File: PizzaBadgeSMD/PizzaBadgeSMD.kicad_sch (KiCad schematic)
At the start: 168 parts, among them J1 BAT -, J2 BAT +, Q1 NPN, Q2 NPN, Q3 NPN, Q4 NPN, Q5 NPN, Q6 NPN, Q7 NPN, Q8 NPN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

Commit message: update SMD version
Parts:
- added R82, R83: 10K, Resistor_SMD:R_0805_2012Metric, symbol Device:R
- Q1, Q2, Q3, Q4, Q5, Q6, Q7, Q8: symbol Device:Q_NPN_EBC -> Device:Q_NPN_BEC
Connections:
- net 3.3V: now also R82.1
- net GND: now also R83.2
- net SLICE_8: now also R83.1
- net at R61.2, R62.2, R63.2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: now also Q7.2 (E); no longer Q7.1 (E)
- net at R71.2, R72.2, R73.2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: now also Q8.2 (E); no longer Q8.1 (E)
- net at R80.1: now also Q8.1 (B); no longer Q8.2 (B)
- net at R30.1: now also Q3.1 (B); no longer Q3.2 (B)
- net at R39.1: now also Q4.1 (B); no longer Q4.2 (B)
- net at R41.2, R42.2, R43.2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: now also Q5.2 (E); no longer Q5.1 (E)
- net at R21.2, R22.2, R23.2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: now also Q3.2 (E); no longer Q3.1 (E)
- net at R51.2, R52.2, R53.2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: now also Q6.2 (E); no longer Q6.1 (E)
- net at R11.2, R12.2, R13.2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: now also Q2.2 (E); no longer Q2.1 (E)
- net at R20.1: now also Q2.1 (B); no longer Q2.2 (B)
- net at R31.2, R32.2, R33.2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: now also Q4.2 (E); no longer Q4.1 (E)
- net at R50.1: now also Q5.1 (B); no longer Q5.2 (B)
- net at R1.2, R2.2, R3.2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: now also Q1.2 (E); no longer Q1.1 (E)
- net at R60.1: now also Q6.1 (B); no longer Q6.2 (B)
- net at R10.1: now also Q1.1 (B); no longer Q1.2 (B)
- net at R70.1: now also Q7.1 (B); no longer Q7.2 (B)
- net at U1.3 (EN): now also R82.2
- no-connect marks 11 -> 10
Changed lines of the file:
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@@
   (junction (at 143.51 176.53) (diameter 0) (color 0 0 0 0)
   )
+  (junction (at 269.24 146.05) (diameter 0) (color 0 0 0 0)
+  )
   (junction (at 161.29 120.65) (diameter 0) (color 0 0 0 0)
   )
@@
   (no_connect (at 234.95 146.05))
   (no_connect (at 234.95 138.43))
-  (no_connect (at 234.95 128.27))
   (no_connect (at 265.43 130.81))
   (wire (pts (xy 227.33 54.61) (xy 227.33 62.23))
@@
     (stroke (width 0) (type default) (color 0 0 0 0))
   )
+  (wire (pts (xy 269.24 146.05) (xy 269.24 152.4))
+    (stroke (width 0) (type default) (color 0 0 0 0))
+  )
   (wire (pts (xy 21.59 29.21) (xy 21.59 36.83))
     (stroke (width 0) (type default) (color 0 0 0 0))
@@
     (stroke (width 0) (type default) (color 0 0 0 0))
   )
+  (wire (pts (xy 279.4 152.4) (xy 276.86 152.4))
+    (stroke (width 0) (type default) (color 0 0 0 0))
+  )
   (wire (pts (xy 123.19 29.21) (xy 121.92 29.21))
     (stroke (width 0) (type default) (color 0 0 0 0))
@@
     (stroke (width 0) (type default) (color 0 0 0 0))
   )
+  (wire (pts (xy 269.24 146.05) (xy 265.43 146.05))
+    (stroke (width 0) (type default) (color 0 0 0 0))
+  )
   (wire (pts (xy 71.12 85.09) (xy 69.85 85.09))
     (stroke (width 0) (type default) (color 0 0 0 0))
@@
     (stroke (width 0) (type default) (color 0 0 0 0))
   )
+  (wire (pts (xy 271.78 146.05) (xy 269.24 146.05))
+    (stroke (width 0) (type default) (color 0 0 0 0))
+  )
   (wire (pts (xy 92.71 134.62) (xy 93.98 134.62))
     (stroke (width 0) (type default) (color 0 0 0 0))
@@
     (stroke (width 0) (type default) (color 0 0 0 0))
   )
+  (global_label "3.3V" (shape input) (at 227.33 128.27 180) (fields_autoplaced)
+    (effects (font (size 1.27 1.27)) (justify right))
+    (property "Intersheet References" "${INTERSHEET_REFS}" (id 0) (at 220.8045 128.3494 0)
+      (effects (font (size 1.27 1.27)) (justify right) hide)
+    )
+  )
   (global_label "GND" (shape input) (at 69.85 90.17 180) (fields_autoplaced)
     (effects (font (size 1.27 1.27)) (justify right))
@@
     )
   )
+  (global_label "GND" (shape input) (at 279.4 152.4 270) (fields_autoplaced)
+    (effects (font (size 1.27 1.27)) (justify right))
+    (property "Intersheet References" "${INTERSHEET_REFS}" (id 0) (at 279.3206 158.6836 90)
+      (effects (font (size 1.27 1.27)) (justify right) hide)
+    )
+  )
   (global_label "SLICE_3" (shape input) (at 265.43 123.19 0) (fields_autoplaced)
     (effects (font (size 1.27 1.27)) (justify left))
@@
     )
   )
-  (global_label "SLICE_8" (shape input) (at 265.43 146.05 0) (fields_autoplaced)
+  (global_label "SLICE_8" (shape input) (at 271.78 146.05 0) (fields_autoplaced)
     (effects (font (size 1.27 1.27)) (justify left))
-    (property "Intersheet References" "${INTERSHEET_REFS}" (id 0) (at 275.2817 145.9706 0)
+    (property "Intersheet References" "${INTERSHEET_REFS}" (id 0) (at 281.6317 145.9706 0)
       (effects (font (size 1.27 1.27)) (justify left) hide)
     )
@@
     (pin "2")
   )
-  (symbol (lib_id "Device:Q_NPN_EBC") (at 167.64 140.97 270) (unit 1)
+  (symbol (lib_id "Device:Q_NPN_BEC") (at 167.64 140.97 270) (unit 1)
     (in_bom yes) (on_board yes) (fields_autoplaced)
     (property "Reference" "Q8" (id 0) (at 167.64 147.32 90))
@@
     (pin "2")
   )
-  (symbol (lib_id "Device:Q_NPN_EBC") (at 96.52 49.53 270) (unit 1)
+  (symbol (lib_id "Device:Q_NPN_BEC") (at 96.52 49.53 270) (unit 1)
     (in_bom yes) (on_board yes) (fields_autoplaced)
     (property "Reference" "Q2" (id 0) (at 96.52 55.88 90))
@@
     (pin "2")
   )
-  (symbol (lib_id "Device:Q_NPN_EBC") (at 194.31 49.53 270) (unit 1)
+  (symbol (lib_id "Device:Q_NPN_BEC") (at 194.31 49.53 270) (unit 1)
     (in_bom yes) (on_board yes) (fields_autoplaced)
     (property "Reference" "Q4" (id 0) (at 194.31 55.88 90))
@@
     (pin "1")
   )
-  (symbol (lib_id "Device:Q_NPN_EBC") (at 146.05 49.53 270) (unit 1)
+  (symbol (lib_id "Device:Q_NPN_BEC") (at 146.05 49.53 270) (unit 1)
     (in_bom yes) (on_board yes) (fields_autoplaced)
     (property "Reference" "Q3" (id 0) (at 146.05 55.88 90))
@@
     (pin "2")
   )
-  (symbol (lib_id "Device:Q_NPN_EBC") (at 251.46 52.07 270) (unit 1)
+  (symbol (lib_id "Device:Q_NPN_BEC") (at 251.46 52.07 270) (unit 1)
     (in_bom yes) (on_board yes) (fields_autoplaced)
     (property "Reference" "Q5" (id 0) (at 251.46 58.42 90))
@@
     (pin "2")
   )
-  (symbol (lib_id "Device:Q_NPN_EBC") (at 54.61 139.7 270) (unit 1)
+  (symbol (lib_id "Device:Q_NPN_BEC") (at 54.61 139.7 270) (unit 1)
     (in_bom yes) (on_board yes) (fields_autoplaced)
     (property "Reference" "Q6" (id 0) (at 54.61 146.05 90))
@@
     (pin "2")
   )
-  (symbol (lib_id "Device:Q_NPN_EBC") (at 107.95 139.7 270) (unit 1)
+  (symbol (lib_id "Device:Q_NPN_BEC") (at 107.95 139.7 270) (unit 1)
     (in_bom yes) (on_board yes) (fields_autoplaced)
     (property "Reference" "Q7" (id 0) (at 107.95 146.05 90))
@@
     (pin "2")
   )
-  (symbol (lib_id "Device:Q_NPN_EBC") (at 46.99 49.53 270) (unit 1)
+  (symbol (lib_id "Device:Q_NPN_BEC") (at 46.99 49.53 270) (unit 1)
     (in_bom yes) (on_board yes) (fields_autoplaced)
     (property "Reference" "Q1" (id 0) (at 46.99 55.88 90))
@@
     (pin "2")
   )
+  (symbol (lib_id "Device:R") (at 231.14 128.27 90) (unit 1)
+    (in_bom yes) (on_board yes)
+    (property "Reference" "R82" (id 0) (at 231.14 125.73 90))
+    (property "Value" "10K" (id 1) (at 231.14 128.27 90))
+    (property "Footprint" "Resistor_SMD:R_0805_2012Metric" (id 2) (at 231.14 130.048 90)
+      (effects (font (size 1.27 1.27)) hide)
+    )
+    (property "Datasheet" "~" (id 3) (at 231.14 128.27 0)
+      (effects (font (size 1.27 1.27)) hide)
+    )
+    (pin "1")
+    (pin "2")
+  )
   (symbol (lib_id "Device:R") (at 44.45 149.86 90) (unit 1)
     (in_bom yes) (on_board yes)
@@
     (pin "2")
   )
+  (symbol (lib_id "Device:R") (at 273.05 152.4 90) (unit 1)
+    (in_bom yes) (on_board yes)
+    (property "Reference" "R83" (id 0) (at 273.05 149.86 90))
+    (property "Value" "10K" (id 1) (at 273.05 152.4 90))
+    (property "Footprint" "Resistor_SMD:R_0805_2012Metric" (id 2) (at 273.05 154.178 90)
+      (effects (font (size 1.27 1.27)) hide)
+    )
+    (property "Datasheet" "~" (id 3) (at 273.05 152.4 0)
+      (effects (font (size 1.27 1.27)) hide)
+    )
+    (pin "1")
+    (pin "2")
+  )
   (symbol (lib_id "Device:R") (at 157.48 167.64 90) (unit 1)
     (in_bom yes) (on_board yes)
@@
       (reference "R81") (unit 1) (value "10K") (footprint "Resistor_SMD:R_0805_2012Metric")
     )
+    (path "/f0d89eae-86d0-4eee-82c6-ad3daf7543e5"
+      (reference "R82") (unit 1) (value "10K") (footprint "Resistor_SMD:R_0805_2012Metric")
+    )
+    (path "/f377b136-56b5-4e23-8cd2-f732b5942e28"
+      (reference "R83") (unit 1) (value "10K") (footprint "Resistor_SMD:R_0805_2012Metric")
+    )
     (path "/ed6cd72f-4985-4265-a8c6-e1402f632187"

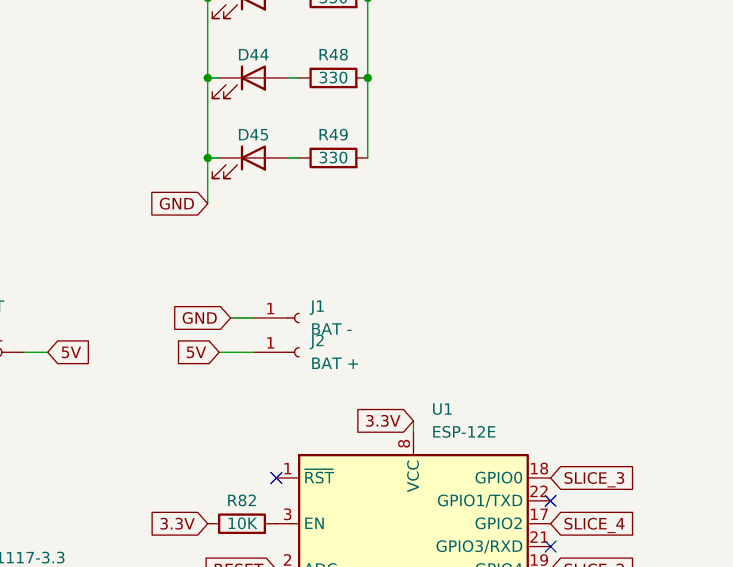
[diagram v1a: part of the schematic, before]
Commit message: add coin battery
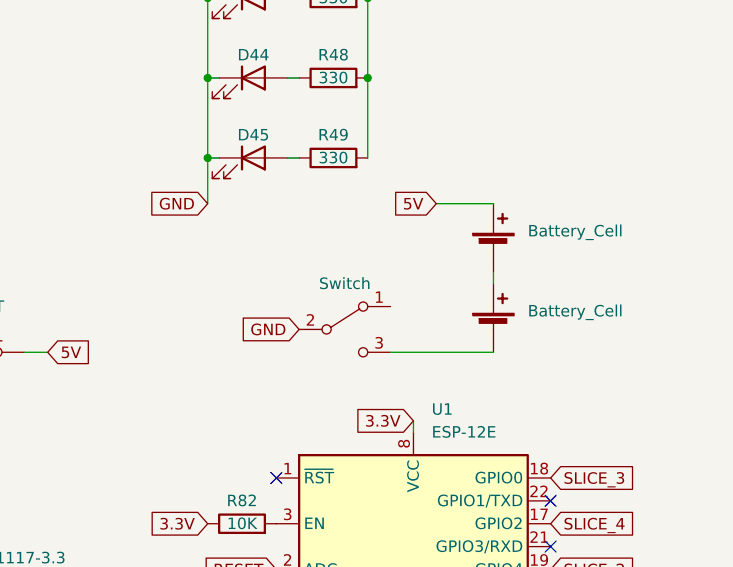
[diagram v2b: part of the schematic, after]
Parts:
- removed J1: BAT -, TestPoint:TestPoint_Pad_3.0x3.0mm, symbol Connector:Conn_01x01_Female
- removed J2: BAT +, TestPoint:TestPoint_Pad_3.0x3.0mm, symbol Connector:Conn_01x01_Female
- added BT1, BT2: Battery_Cell, Battery:BatteryHolder_Keystone_3000_1x12mm, symbol Device:Battery_Cell
- added SW2: Switch, Button_Switch_SMD:SW_SPDT_CK-JS102011SAQN, symbol Switch:SW_SPDT
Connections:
- net 5V: now also BT1.1 (+)
- net GND: now also SW2.2 (B)
- new net: BT1.2 (-), BT2.1 (+)
- new net: BT2.2 (-), SW2.3 (C)
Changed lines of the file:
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@@
     (stroke (width 0) (type default) (color 0 0 0 0))
   )
+  (wire (pts (xy 259.08 100.33) (xy 259.08 101.6))
+    (stroke (width 0) (type default) (color 0 0 0 0))
+  )
   (wire (pts (xy 78.74 67.31) (xy 80.01 67.31))
     (stroke (width 0) (type default) (color 0 0 0 0))
@@
     (stroke (width 0) (type default) (color 0 0 0 0))
   )
+  (wire (pts (xy 252.73 92.71) (xy 259.08 92.71))
+    (stroke (width 0) (type default) (color 0 0 0 0))
+  )
   (wire (pts (xy 170.18 44.45) (xy 170.18 52.07))
     (stroke (width 0) (type default) (color 0 0 0 0))
@@
     (stroke (width 0) (type default) (color 0 0 0 0))
   )
-  (wire (pts (xy 229.87 105.41) (xy 232.41 105.41))
-    (stroke (width 0) (type default) (color 0 0 0 0))
-  )
   (wire (pts (xy 205.74 143.51) (xy 205.74 146.05))
     (stroke (width 0) (type default) (color 0 0 0 0))
@@
     (stroke (width 0) (type default) (color 0 0 0 0))
   )
-  (wire (pts (xy 228.6 109.22) (xy 232.41 109.22))
-    (stroke (width 0) (type default) (color 0 0 0 0))
-  )
   (wire (pts (xy 101.6 166.37) (xy 101.6 175.26))
     (stroke (width 0) (type default) (color 0 0 0 0))
@@
     (stroke (width 0) (type default) (color 0 0 0 0))
   )
+  (wire (pts (xy 247.65 109.22) (xy 259.08 109.22))
+    (stroke (width 0) (type default) (color 0 0 0 0))
+  )
   (wire (pts (xy 78.74 29.21) (xy 80.01 29.21))
     (stroke (width 0) (type default) (color 0 0 0 0))
@@
     )
   )
-  (global_label "GND" (shape input) (at 229.87 105.41 180) (fields_autoplaced)
+  (global_label "GND" (shape input) (at 237.49 106.68 180) (fields_autoplaced)
     (effects (font (size 1.27 1.27)) (justify right))
-    (property "Intersheet References" "${INTERSHEET_REFS}" (id 0) (at 223.5864 105.3306 0)
+    (property "Intersheet References" "${INTERSHEET_REFS}" (id 0) (at 231.2064 106.6006 0)
       (effects (font (size 1.27 1.27)) (justify right) hide)
     )
@@
     )
   )
-  (global_label "5V" (shape input) (at 228.6 109.22 180) (fields_autoplaced)
+  (global_label "5V" (shape input) (at 252.73 92.71 180) (fields_autoplaced)
     (effects (font (size 1.27 1.27)) (justify right))
-    (property "Intersheet References" "${INTERSHEET_REFS}" (id 0) (at 223.8888 109.1406 0)
+    (property "Intersheet References" "${INTERSHEET_REFS}" (id 0) (at 248.0188 92.6306 0)
       (effects (font (size 1.27 1.27)) (justify right) hide)
     )
@@
     (pin "2")
   )
-  (symbol (lib_id "Connector:Conn_01x01_Female") (at 237.49 109.22 0) (unit 1)
-    (in_bom yes) (on_board yes) (fields_autoplaced)
-    (property "Reference" "J2" (id 0) (at 238.76 107.9499 0)
-      (effects (font (size 1.27 1.27)) (justify left))
-    )
-    (property "Value" "BAT +" (id 1) (at 238.76 110.4899 0)
-      (effects (font (size 1.27 1.27)) (justify left))
-    )
-    (property "Footprint" "TestPoint:TestPoint_Pad_3.0x3.0mm" (id 2) (at 237.49 109.22 0)
-      (effects (font (size 1.27 1.27)) hide)
-    )
-    (property "Datasheet" "~" (id 3) (at 237.49 109.22 0)
-      (effects (font (size 1.27 1.27)) hide)
-    )
-    (pin "1")
-  )
   (symbol (lib_id "Device:Q_NPN_BEC") (at 146.05 49.53 270) (unit 1)
     (in_bom yes) (on_board yes) (fields_autoplaced)
@@
     (pin "2")
   )
+  (symbol (lib_id "Device:Battery_Cell") (at 259.08 97.79 0) (unit 1)
+    (in_bom yes) (on_board yes) (fields_autoplaced)
+    (property "Reference" "BT1" (id 0) (at 262.89 94.4879 0)
+      (effects (font (size 1.27 1.27)) (justify left) hide)
+    )
+    (property "Value" "Battery_Cell" (id 1) (at 262.89 95.7579 0)
+      (effects (font (size 1.27 1.27)) (justify left))
+    )
+    (property "Footprint" "Battery:BatteryHolder_Keystone_3000_1x12mm" (id 2) (at 259.08 96.266 90)
+      (effects (font (size 1.27 1.27)) hide)
+    )
+    (property "Datasheet" "~" (id 3) (at 259.08 96.266 90)
+      (effects (font (size 1.27 1.27)) hide)
+    )
+    (pin "1")
+    (pin "2")
+  )
   (symbol (lib_id "Device:R") (at 58.42 132.08 90) (unit 1)
     (in_bom yes) (on_board yes)
@@
     (pin "2")
   )
-  (symbol (lib_id "Connector:Conn_01x01_Female") (at 237.49 105.41 0) (unit 1)
-    (in_bom yes) (on_board yes) (fields_autoplaced)
-    (property "Reference" "J1" (id 0) (at 238.76 104.1399 0)
-      (effects (font (size 1.27 1.27)) (justify left))
-    )
-    (property "Value" "BAT -" (id 1) (at 238.76 106.6799 0)
-      (effects (font (size 1.27 1.27)) (justify left))
-    )
-    (property "Footprint" "TestPoint:TestPoint_Pad_3.0x3.0mm" (id 2) (at 237.49 105.41 0)
-      (effects (font (size 1.27 1.27)) hide)
-    )
-    (property "Datasheet" "~" (id 3) (at 237.49 105.41 0)
-      (effects (font (size 1.27 1.27)) hide)
-    )
-    (pin "1")
-  )
   (symbol (lib_id "Device:LED") (at 175.26 44.45 0) (unit 1)
     (in_bom yes) (on_board yes)
@@
     (pin "2")
   )
+  (symbol (lib_id "Device:Battery_Cell") (at 259.08 106.68 0) (unit 1)
+    (in_bom yes) (on_board yes) (fields_autoplaced)
+    (property "Reference" "BT2" (id 0) (at 262.89 103.3779 0)
+      (effects (font (size 1.27 1.27)) (justify left) hide)
+    )
+    (property "Value" "Battery_Cell" (id 1) (at 262.89 104.6479 0)
+      (effects (font (size 1.27 1.27)) (justify left))
+    )
+    (property "Footprint" "Battery:BatteryHolder_Keystone_3000_1x12mm" (id 2) (at 259.08 105.156 90)
+      (effects (font (size 1.27 1.27)) hide)
+    )
+    (property "Datasheet" "~" (id 3) (at 259.08 105.156 90)
+      (effects (font (size 1.27 1.27)) hide)
+    )
+    (pin "1")
+    (pin "2")
+  )
   (symbol (lib_id "Device:LED") (at 35.56 119.38 0) (unit 1)
     (in_bom yes) (on_board yes)
@@
     (pin "2")
   )
+  (symbol (lib_id "Switch:SW_SPDT") (at 242.57 106.68 0) (unit 1)
+    (in_bom yes) (on_board yes) (fields_autoplaced)
+    (property "Reference" "SW2" (id 0) (at 242.57 101.6 0)
+      (effects (font (size 1.27 1.27)) hide)
+    )
+    (property "Value" "Switch" (id 1) (at 242.57 101.6 0))
+    (property "Footprint" "Button_Switch_SMD:SW_SPDT_CK-JS102011SAQN" (id 2) (at 242.57 106.68 0)
+      (effects (font (size 1.27 1.27)) hide)
+    )
+    (property "Datasheet" "~" (id 3) (at 242.57 106.68 0)
+      (effects (font (size 1.27 1.27)) hide)
+    )
+    (pin "1")
+    (pin "2")
+    (pin "3")
+  )
   (symbol (lib_id "Device:R") (at 157.48 167.64 90) (unit 1)
     (in_bom yes) (on_board yes)
@@
   )
   (symbol_instances
+    (path "/6c827c18-fa9e-48ed-ae59-de7f06672e71"
+      (reference "BT1") (unit 1) (value "Battery_Cell") (footprint "Battery:BatteryHolder_Keystone_3000_1x12mm")
+    )
+    (path "/d7672da8-9302-4479-abcf-93a65f594d80"
+      (reference "BT2") (unit 1) (value "Battery_Cell") (footprint "Battery:BatteryHolder_Keystone_3000_1x12mm")
+    )
     (path "/d4fba0db-5d79-4a75-b55a-6213bf0452ed"
       (reference "C1") (unit 1) (value "1uF") (footprint "Capacitor_SMD:C_0805_2012Metric")
@@
       (reference "D72") (unit 1) (value "LED") (footprint "LED_SMD:LED_0805_2012Metric")
     )
-    (path "/cea002a4-2d4e-4eb1-abfb-142158fc8b9d"
-      (reference "J1") (unit 1) (value "BAT -") (footprint "TestPoint:TestPoint_Pad_3.0x3.0mm")
-    )
-    (path "/42765826-837e-4375-ad5d-c11d8588d303"
-      (reference "J2") (unit 1) (value "BAT +") (footprint "TestPoint:TestPoint_Pad_3.0x3.0mm")
-    )
     (path "/86e1da85-bdb0-4d78-b747-ecb447b1b842"
       (reference "Q1") (unit 1) (value "NPN") (footprint "Package_TO_SOT_SMD:SOT-23")
@@
       (reference "SW1") (unit 1) (value "RESET") (footprint "Button_Switch_SMD:SW_SPST_CK_RS282G05A3")
     )
+    (path "/f4cc036a-96d3-4325-b01d-b9d5c6a6df17"
+      (reference "SW2") (unit 1) (value "Switch") (footprint "Button_Switch_SMD:SW_SPDT_CK-JS102011SAQN")
+    )
     (path "/dc1328ae-788e-4e55-8090-8d0fa272fa94"

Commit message: change switch button
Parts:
- SW2: footprint Button_Switch_SMD:SW_SPDT_CK-JS102011SAQN -> Button_Switch_SMD:SW_SPDT_PCM12
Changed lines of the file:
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@@
     )
     (property "Value" "Switch" (id 1) (at 242.57 101.6 0))
-    (property "Footprint" "Button_Switch_SMD:SW_SPDT_CK-JS102011SAQN" (id 2) (at 242.57 106.68 0)
+    (property "Footprint" "Button_Switch_SMD:SW_SPDT_PCM12" (id 2) (at 242.57 106.68 0)
       (effects (font (size 1.27 1.27)) hide)
     )
@@
     )
     (path "/f4cc036a-96d3-4325-b01d-b9d5c6a6df17"
-      (reference "SW2") (unit 1) (value "Switch") (footprint "Button_Switch_SMD:SW_SPDT_CK-JS102011SAQN")
+      (reference "SW2") (unit 1) (value "Switch") (footprint "Button_Switch_SMD:SW_SPDT_PCM12")
     )
     (path "/dc1328ae-788e-4e55-8090-8d0fa272fa94"
